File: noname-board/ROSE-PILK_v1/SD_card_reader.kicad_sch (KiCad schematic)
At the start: 1 part, among them J5 Conn_02x08_Row_Letter_First

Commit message: SD Card Stuff
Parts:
- removed J5: Conn_02x08_Row_Letter_First, Connector_PinSocket_2.54mm:PinSocket_2x08_P2.54mm_Vertical, symbol Connector_Generic:Conn_02x08_Row_Letter_First
- added J7: Conn_02x08_Row_Letter_Last, symbol Connector_Generic:Conn_02x08_Row_Letter_Last
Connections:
- new net 3V3: J7.2a (Pin_2a), J7.2b (Pin_2b)
- new net 5V: J7.3a (Pin_3a), J7.3b (Pin_3b)
- new net CS: J7.4a (Pin_4a), J7.4b (Pin_4b)
- new net GND: J7.1a (Pin_1a), J7.1b (Pin_1b), J7.8a (Pin_8a), J7.8b (Pin_8b)
- new net MISO: J7.7a (Pin_7a), J7.7b (Pin_7b)
- new net MOSI: J7.5a (Pin_5a), J7.5b (Pin_5b)
- new net SCK: J7.6a (Pin_6a), J7.6b (Pin_6b)
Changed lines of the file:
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@@
 (kicad_sch (version 20230121) (generator eeschema)
   (paper "A4")
+  )
   (bus_entry (at 149.86 138.43) (size 2.54 2.54)
     (stroke (width 0) (type default))
   )
-  (symbol (lib_id "Connector_Generic:Conn_02x08_Row_Letter_First") (at 148.59 81.28 0) (unit 1)
+  (wire (pts (xy 129.54 120.65) (xy 134.62 120.65))
+    (stroke (width 0) (type default))
+  )
+  (wire (pts (xy 111.76 123.19) (xy 116.84 123.19))
+    (stroke (width 0) (type default))
+  )
+  (wire (pts (xy 129.54 130.81) (xy 134.62 130.81))
+    (stroke (width 0) (type default))
+  )
+  (wire (pts (xy 111.76 130.81) (xy 116.84 130.81))
+    (stroke (width 0) (type default))
+  )
+  (wire (pts (xy 129.54 123.19) (xy 134.62 123.19))
+    (stroke (width 0) (type default))
+  )
+  (wire (pts (xy 129.54 125.73) (xy 134.62 125.73))
+    (stroke (width 0) (type default))
+  )
+  (wire (pts (xy 129.54 128.27) (xy 134.62 128.27))
+    (stroke (width 0) (type default))
+  )
+  (wire (pts (xy 129.54 118.11) (xy 134.62 118.11))
+    (stroke (width 0) (type default))
+  )
+  (wire (pts (xy 129.54 135.89) (xy 134.62 135.89))
+    (stroke (width 0) (type default))
+  )
+  (wire (pts (xy 111.76 133.35) (xy 116.84 133.35))
+    (stroke (width 0) (type default))
+  )
+  (wire (pts (xy 111.76 128.27) (xy 116.84 128.27))
+    (stroke (width 0) (type default))
+  )
+  (wire (pts (xy 111.76 118.11) (xy 116.84 118.11))
+    (stroke (width 0) (type default))
+  )
+  (wire (pts (xy 111.76 125.73) (xy 116.84 125.73))
+    (stroke (width 0) (type default))
+  )
+  (wire (pts (xy 111.76 120.65) (xy 116.84 120.65))
+    (stroke (width 0) (type default))
+  )
+  (wire (pts (xy 129.54 133.35) (xy 134.62 133.35))
+    (stroke (width 0) (type default))
+  )
+  (wire (pts (xy 111.76 135.89) (xy 116.84 135.89))
+    (stroke (width 0) (type default))
+  )
+  (hierarchical_label "GND" (shape input) (at 111.76 135.89 180) (fields_autoplaced)
+    (effects (font (size 1.27 1.27)) (justify right))
+  )
+  (hierarchical_label "GND" (shape input) (at 134.62 135.89 0) (fields_autoplaced)
+    (effects (font (size 1.27 1.27)) (justify left))
+  )
+  (hierarchical_label "MISO" (shape input) (at 134.62 133.35 0) (fields_autoplaced)
+    (effects (font (size 1.27 1.27)) (justify left))
+  )
+  (hierarchical_label "MOSI" (shape input) (at 134.62 128.27 0) (fields_autoplaced)
+    (effects (font (size 1.27 1.27)) (justify left))
+  )
+  (hierarchical_label "SCK" (shape input) (at 134.62 130.81 0) (fields_autoplaced)
+    (effects (font (size 1.27 1.27)) (justify left))
+  )
+  (hierarchical_label "GND" (shape input) (at 111.76 118.11 180) (fields_autoplaced)
+    (effects (font (size 1.27 1.27)) (justify right))
+  )
+  (hierarchical_label "SCK" (shape input) (at 111.76 130.81 180) (fields_autoplaced)
+    (effects (font (size 1.27 1.27)) (justify right))
+  )
+  (hierarchical_label "MISO" (shape input) (at 111.76 133.35 180) (fields_autoplaced)
+    (effects (font (size 1.27 1.27)) (justify right))
+  )
+  (hierarchical_label "3V3" (shape input) (at 134.62 120.65 0) (fields_autoplaced)
+    (effects (font (size 1.27 1.27)) (justify left))
+  )
+  (hierarchical_label "3V3" (shape input) (at 111.76 120.65 180) (fields_autoplaced)
+    (effects (font (size 1.27 1.27)) (justify right))
+  )
+  (hierarchical_label "GND" (shape input) (at 134.62 118.11 0) (fields_autoplaced)
+    (effects (font (size 1.27 1.27)) (justify left))
+  )
+  (hierarchical_label "CS" (shape input) (at 111.76 125.73 180) (fields_autoplaced)
+    (effects (font (size 1.27 1.27)) (justify right))
+  )
+  (hierarchical_label "5V" (shape input) (at 134.62 123.19 0) (fields_autoplaced)
+    (effects (font (size 1.27 1.27)) (justify left))
+  )
+  (hierarchical_label "5V" (shape input) (at 111.76 123.19 180) (fields_autoplaced)
+    (effects (font (size 1.27 1.27)) (justify right))
+  )
+  (hierarchical_label "CS" (shape input) (at 134.62 125.73 0) (fields_autoplaced)
+    (effects (font (size 1.27 1.27)) (justify left))
+  )
+  (hierarchical_label "MOSI" (shape input) (at 111.76 128.27 180) (fields_autoplaced)
+    (effects (font (size 1.27 1.27)) (justify right))
+  )
+  (symbol (lib_id "Connector_Generic:Conn_02x08_Row_Letter_Last") (at 121.92 125.73 0) (unit 1)
     (in_bom yes) (on_board yes) (dnp no) (fields_autoplaced)
-    (property "Reference" "J5" (at 149.86 67.31 0)
+    (property "Reference" "J7" (at 123.19 111.76 0)
       (effects (font (size 1.27 1.27)))
     )
-    (property "Value" "Conn_02x08_Row_Letter_First" (at 149.86 69.85 0)
+    (property "Value" "Conn_02x08_Row_Letter_Last" (at 123.19 114.3 0)
       (effects (font (size 1.27 1.27)))
     )
-    (property "Footprint" "Connector_PinSocket_2.54mm:PinSocket_2x08_P2.54mm_Vertical" (at 148.59 81.28 0)
+    (property "Footprint" "" (at 121.92 125.73 0)
       (effects (font (size 1.27 1.27)) hide)
     )
-    (property "Datasheet" "~" (at 148.59 81.28 0)
+    (property "Datasheet" "~" (at 121.92 125.73 0)
       (effects (font (size 1.27 1.27)) hide)
     )
-    (pin "a1")
-    (pin "a2")
-    (pin "a3")
-    (pin "a4")
-    (pin "a5")
-    (pin "a6")
-    (pin "a7")
-    (pin "a8")
-    (pin "b1")
-    (pin "b2")
-    (pin "b3")
-    (pin "b4")
-    (pin "b5")
-    (pin "b6")
-    (pin "b7")
-    (pin "b8")
+    (pin "1a")
+    (pin "1b")
+    (pin "2a")
+    (pin "2b")
+    (pin "3a")
+    (pin "3b")
+    (pin "4a")
+    (pin "4b")
+    (pin "5a")
+    (pin "5b")
+    (pin "6a")
+    (pin "6b")
+    (pin "7a")
+    (pin "7b")
+    (pin "8a")
+    (pin "8b")
     (instances
       (project "ROSE-PILK_v1"
         (path "/3dfb9737-68ba-4ca9-8085-72e4f57f9e50/bba6feb6-0708-4b51-a731-0bb8ba53ae80"
-          (reference "J5") (unit 1)
+          (reference "J7") (unit 1)
         )
       )

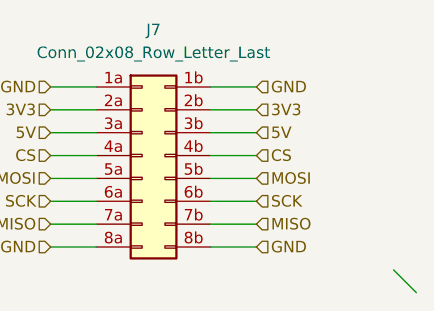
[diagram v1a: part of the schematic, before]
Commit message: Footprint Assignments
Assigned footprints to things that didn't currently have ones
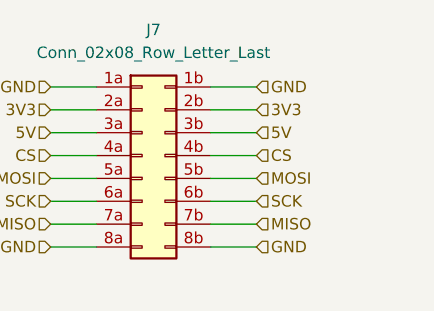
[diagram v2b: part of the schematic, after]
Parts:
- J7: footprint (none) -> Connector_PinSocket_2.00mm:PinSocket_2x08_P2.00mm_Vertical
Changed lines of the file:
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@@
   (paper "A4")
-  )
-  (bus_entry (at 149.86 138.43) (size 2.54 2.54)
-    (stroke (width 0) (type default))
   )
   (wire (pts (xy 129.54 120.65) (xy 134.62 120.65))
@@
       (effects (font (size 1.27 1.27)))
     )
-    (property "Footprint" "" (at 121.92 125.73 0)
+    (property "Footprint" "Connector_PinSocket_2.00mm:PinSocket_2x08_P2.00mm_Vertical" (at 121.92 125.73 0)
       (effects (font (size 1.27 1.27)) hide)
     )

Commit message: Meeting Stuff
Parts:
- removed J7: Conn_02x08_Row_Letter_Last, Connector_PinSocket_2.00mm:PinSocket_2x08_P2.00mm_Vertical, symbol Connector_Generic:Conn_02x08_Row_Letter_Last
- added J5: Conn_02x08_Odd_Even, Connector_PinSocket_2.00mm:PinSocket_2x08_P2.00mm_Vertical, symbol Connector_Generic:Conn_02x08_Odd_Even
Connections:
- net 3V3: now also J5.3 (Pin_3), J5.4 (Pin_4)
- net 5V: now also J5.5 (Pin_5), J5.6 (Pin_6)
- net CS: now also J5.7 (Pin_7), J5.8 (Pin_8)
- net GND: now also J5.1 (Pin_1), J5.15 (Pin_15), J5.16 (Pin_16), J5.2 (Pin_2)
- net MISO: now also J5.13 (Pin_13), J5.14 (Pin_14)
- net MOSI: now also J5.10 (Pin_10), J5.9 (Pin_9)
- net SCK: now also J5.11 (Pin_11), J5.12 (Pin_12)
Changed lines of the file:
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@@
 (kicad_sch (version 20230121) (generator eeschema)
   (paper "A4")
-  )
   (wire (pts (xy 129.54 120.65) (xy 134.62 120.65))
     (stroke (width 0) (type default))
@@
     (stroke (width 0) (type default))
   )
-  (wire (pts (xy 129.54 130.81) (xy 134.62 130.81))
+  (wire (pts (xy 129.54 118.11) (xy 134.62 118.11))
+    (stroke (width 0) (type default))
+  )
+  (wire (pts (xy 129.54 123.19) (xy 134.62 123.19))
+    (stroke (width 0) (type default))
+  )
+  (wire (pts (xy 129.54 133.35) (xy 134.62 133.35))
     (stroke (width 0) (type default))
   )
@@
     (stroke (width 0) (type default))
   )
-  (wire (pts (xy 129.54 123.19) (xy 134.62 123.19))
-    (stroke (width 0) (type default))
-  )
   (wire (pts (xy 129.54 125.73) (xy 134.62 125.73))
     (stroke (width 0) (type default))
   )
-  (wire (pts (xy 129.54 128.27) (xy 134.62 128.27))
+  (wire (pts (xy 129.54 130.81) (xy 134.62 130.81))
     (stroke (width 0) (type default))
   )
-  (wire (pts (xy 129.54 118.11) (xy 134.62 118.11))
+  (wire (pts (xy 129.54 128.27) (xy 134.62 128.27))
     (stroke (width 0) (type default))
   )
@@
   )
   (wire (pts (xy 111.76 120.65) (xy 116.84 120.65))
-    (stroke (width 0) (type default))
-  )
-  (wire (pts (xy 129.54 133.35) (xy 134.62 133.35))
     (stroke (width 0) (type default))
   )
@@
     (effects (font (size 1.27 1.27)) (justify right))
   )
-  (symbol (lib_id "Connector_Generic:Conn_02x08_Row_Letter_Last") (at 121.92 125.73 0) (unit 1)
+  (symbol (lib_id "Connector_Generic:Conn_02x08_Odd_Even") (at 121.92 125.73 0) (unit 1)
     (in_bom yes) (on_board yes) (dnp no) (fields_autoplaced)
-    (property "Reference" "J7" (at 123.19 111.76 0)
+    (property "Reference" "J5" (at 123.19 111.76 0)
       (effects (font (size 1.27 1.27)))
     )
-    (property "Value" "Conn_02x08_Row_Letter_Last" (at 123.19 114.3 0)
+    (property "Value" "Conn_02x08_Odd_Even" (at 123.19 114.3 0)
       (effects (font (size 1.27 1.27)))
     )
@@
       (effects (font (size 1.27 1.27)) hide)
     )
-    (pin "1a")
-    (pin "1b")
-    (pin "2a")
-    (pin "2b")
-    (pin "3a")
-    (pin "3b")
-    (pin "4a")
-    (pin "4b")
-    (pin "5a")
-    (pin "5b")
-    (pin "6a")
-    (pin "6b")
-    (pin "7a")
-    (pin "7b")
-    (pin "8a")
-    (pin "8b")
+    (pin "1")
+    (pin "10")
+    (pin "11")
+    (pin "12")
+    (pin "13")
+    (pin "14")
+    (pin "15")
+    (pin "16")
+    (pin "2")
+    (pin "3")
+    (pin "4")
+    (pin "5")
+    (pin "6")
+    (pin "7")
+    (pin "8")
+    (pin "9")
     (instances
       (project "ROSE-PILK_v1"
         (path "/3dfb9737-68ba-4ca9-8085-72e4f57f9e50/bba6feb6-0708-4b51-a731-0bb8ba53ae80"
-          (reference "J7") (unit 1)
+          (reference "J5") (unit 1)
         )
       )

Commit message: Schematics
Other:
- moved on the sheet: J5
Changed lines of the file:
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@@
 (kicad_sch (version 20230121) (generator eeschema)
   (paper "A4")
-  (wire (pts (xy 129.54 120.65) (xy 134.62 120.65))
+  (wire (pts (xy 126.365 130.175) (xy 126.365 135.255))
     (stroke (width 0) (type default))
   )
-  (wire (pts (xy 111.76 123.19) (xy 116.84 123.19))
+  (wire (pts (xy 123.825 112.395) (xy 123.825 117.475))
     (stroke (width 0) (type default))
   )
-  (wire (pts (xy 129.54 118.11) (xy 134.62 118.11))
+  (wire (pts (xy 128.905 130.175) (xy 128.905 135.255))
     (stroke (width 0) (type default))
   )
-  (wire (pts (xy 129.54 123.19) (xy 134.62 123.19))
+  (wire (pts (xy 123.825 130.175) (xy 123.825 135.255))
     (stroke (width 0) (type default))
   )
-  (wire (pts (xy 129.54 133.35) (xy 134.62 133.35))
+  (wire (pts (xy 113.665 130.175) (xy 113.665 135.255))
     (stroke (width 0) (type default))
   )
-  (wire (pts (xy 111.76 130.81) (xy 116.84 130.81))
+  (wire (pts (xy 116.205 112.395) (xy 116.205 117.475))
     (stroke (width 0) (type default))
   )
-  (wire (pts (xy 129.54 125.73) (xy 134.62 125.73))
+  (wire (pts (xy 121.285 130.175) (xy 121.285 135.255))
     (stroke (width 0) (type default))
   )
-  (wire (pts (xy 129.54 130.81) (xy 134.62 130.81))
+  (wire (pts (xy 116.205 130.175) (xy 116.205 135.255))
     (stroke (width 0) (type default))
   )
-  (wire (pts (xy 129.54 128.27) (xy 134.62 128.27))
+  (wire (pts (xy 118.745 130.175) (xy 118.745 135.255))
     (stroke (width 0) (type default))
   )
-  (wire (pts (xy 129.54 135.89) (xy 134.62 135.89))
+  (wire (pts (xy 111.125 130.175) (xy 111.125 135.255))
     (stroke (width 0) (type default))
   )
-  (wire (pts (xy 111.76 133.35) (xy 116.84 133.35))
+  (wire (pts (xy 113.665 112.395) (xy 113.665 117.475))
     (stroke (width 0) (type default))
   )
-  (wire (pts (xy 111.76 128.27) (xy 116.84 128.27))
+  (wire (pts (xy 118.745 112.395) (xy 118.745 117.475))
     (stroke (width 0) (type default))
   )
-  (wire (pts (xy 111.76 118.11) (xy 116.84 118.11))
+  (wire (pts (xy 128.905 112.395) (xy 128.905 117.475))
     (stroke (width 0) (type default))
   )
-  (wire (pts (xy 111.76 125.73) (xy 116.84 125.73))
+  (wire (pts (xy 121.285 112.395) (xy 121.285 117.475))
     (stroke (width 0) (type default))
   )
-  (wire (pts (xy 111.76 120.65) (xy 116.84 120.65))
+  (wire (pts (xy 126.365 112.395) (xy 126.365 117.475))
     (stroke (width 0) (type default))
   )
-  (wire (pts (xy 111.76 135.89) (xy 116.84 135.89))
+  (wire (pts (xy 111.125 112.395) (xy 111.125 117.475))
     (stroke (width 0) (type default))
   )
-  (hierarchical_label "GND" (shape input) (at 111.76 135.89 180) (fields_autoplaced)
+  (hierarchical_label "GND" (shape input) (at 111.125 112.395 90) (fields_autoplaced)
+    (effects (font (size 1.27 1.27)) (justify left))
+  )
+  (hierarchical_label "GND" (shape input) (at 111.125 135.255 270) (fields_autoplaced)
     (effects (font (size 1.27 1.27)) (justify right))
   )
-  (hierarchical_label "GND" (shape input) (at 134.62 135.89 0) (fields_autoplaced)
+  (hierarchical_label "MISO" (shape input) (at 113.665 135.255 270) (fields_autoplaced)
+    (effects (font (size 1.27 1.27)) (justify right))
+  )
+  (hierarchical_label "MOSI" (shape input) (at 118.745 135.255 270) (fields_autoplaced)
+    (effects (font (size 1.27 1.27)) (justify right))
+  )
+  (hierarchical_label "SCK" (shape input) (at 116.205 135.255 270) (fields_autoplaced)
+    (effects (font (size 1.27 1.27)) (justify right))
+  )
+  (hierarchical_label "GND" (shape input) (at 128.905 112.395 90) (fields_autoplaced)
     (effects (font (size 1.27 1.27)) (justify left))
   )
-  (hierarchical_label "MISO" (shape input) (at 134.62 133.35 0) (fields_autoplaced)
+  (hierarchical_label "SCK" (shape input) (at 116.205 112.395 90) (fields_autoplaced)
     (effects (font (size 1.27 1.27)) (justify left))
   )
-  (hierarchical_label "MOSI" (shape input) (at 134.62 128.27 0) (fields_autoplaced)
+  (hierarchical_label "MISO" (shape input) (at 113.665 112.395 90) (fields_autoplaced)
     (effects (font (size 1.27 1.27)) (justify left))
   )
-  (hierarchical_label "SCK" (shape input) (at 134.62 130.81 0) (fields_autoplaced)
+  (hierarchical_label "3V3" (shape input) (at 126.365 135.255 270) (fields_autoplaced)
+    (effects (font (size 1.27 1.27)) (justify right))
+  )
+  (hierarchical_label "3V3" (shape input) (at 126.365 112.395 90) (fields_autoplaced)
     (effects (font (size 1.27 1.27)) (justify left))
   )
-  (hierarchical_label "GND" (shape input) (at 111.76 118.11 180) (fields_autoplaced)
+  (hierarchical_label "GND" (shape input) (at 128.905 135.255 270) (fields_autoplaced)
     (effects (font (size 1.27 1.27)) (justify right))
   )
-  (hierarchical_label "SCK" (shape input) (at 111.76 130.81 180) (fields_autoplaced)
+  (hierarchical_label "CS" (shape input) (at 121.285 112.395 90) (fields_autoplaced)
+    (effects (font (size 1.27 1.27)) (justify left))
+  )
+  (hierarchical_label "5V" (shape input) (at 123.825 135.255 270) (fields_autoplaced)
     (effects (font (size 1.27 1.27)) (justify right))
   )
-  (hierarchical_label "MISO" (shape input) (at 111.76 133.35 180) (fields_autoplaced)
+  (hierarchical_label "5V" (shape input) (at 123.825 112.395 90) (fields_autoplaced)
+    (effects (font (size 1.27 1.27)) (justify left))
+  )
+  (hierarchical_label "CS" (shape input) (at 121.285 135.255 270) (fields_autoplaced)
     (effects (font (size 1.27 1.27)) (justify right))
   )
-  (hierarchical_label "3V3" (shape input) (at 134.62 120.65 0) (fields_autoplaced)
+  (hierarchical_label "MOSI" (shape input) (at 118.745 112.395 90) (fields_autoplaced)
     (effects (font (size 1.27 1.27)) (justify left))
   )
-  (hierarchical_label "3V3" (shape input) (at 111.76 120.65 180) (fields_autoplaced)
-    (effects (font (size 1.27 1.27)) (justify right))
-  )
-  (hierarchical_label "GND" (shape input) (at 134.62 118.11 0) (fields_autoplaced)
-    (effects (font (size 1.27 1.27)) (justify left))
-  )
-  (hierarchical_label "CS" (shape input) (at 111.76 125.73 180) (fields_autoplaced)
-    (effects (font (size 1.27 1.27)) (justify right))
-  )
-  (hierarchical_label "5V" (shape input) (at 134.62 123.19 0) (fields_autoplaced)
-    (effects (font (size 1.27 1.27)) (justify left))
-  )
-  (hierarchical_label "5V" (shape input) (at 111.76 123.19 180) (fields_autoplaced)
-    (effects (font (size 1.27 1.27)) (justify right))
-  )
-  (hierarchical_label "CS" (shape input) (at 134.62 125.73 0) (fields_autoplaced)
-    (effects (font (size 1.27 1.27)) (justify left))
-  )
-  (hierarchical_label "MOSI" (shape input) (at 111.76 128.27 180) (fields_autoplaced)
-    (effects (font (size 1.27 1.27)) (justify right))
-  )
-  (symbol (lib_id "Connector_Generic:Conn_02x08_Odd_Even") (at 121.92 125.73 0) (unit 1)
+  (symbol (lib_id "Connector_Generic:Conn_02x08_Odd_Even") (at 121.285 122.555 270) (unit 1)
     (in_bom yes) (on_board yes) (dnp no) (fields_autoplaced)
-    (property "Reference" "J5" (at 123.19 111.76 0)
+    (property "Reference" "J5" (at 135.255 123.825 0)
       (effects (font (size 1.27 1.27)))
     )
-    (property "Value" "Conn_02x08_Odd_Even" (at 123.19 114.3 0)
+    (property "Value" "Conn_02x08_Odd_Even" (at 132.715 123.825 0)
       (effects (font (size 1.27 1.27)))
     )
-    (property "Footprint" "Connector_PinSocket_2.00mm:PinSocket_2x08_P2.00mm_Vertical" (at 121.92 125.73 0)
+    (property "Footprint" "Connector_PinSocket_2.00mm:PinSocket_2x08_P2.00mm_Vertical" (at 121.285 122.555 0)
       (effects (font (size 1.27 1.27)) hide)
     )
-    (property "Datasheet" "~" (at 121.92 125.73 0)
+    (property "Datasheet" "~" (at 121.285 122.555 0)
       (effects (font (size 1.27 1.27)) hide)
     )
